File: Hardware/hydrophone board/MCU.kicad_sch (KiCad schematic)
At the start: 1 part, among them U601 RASPBERRY_PI_4B_4GB

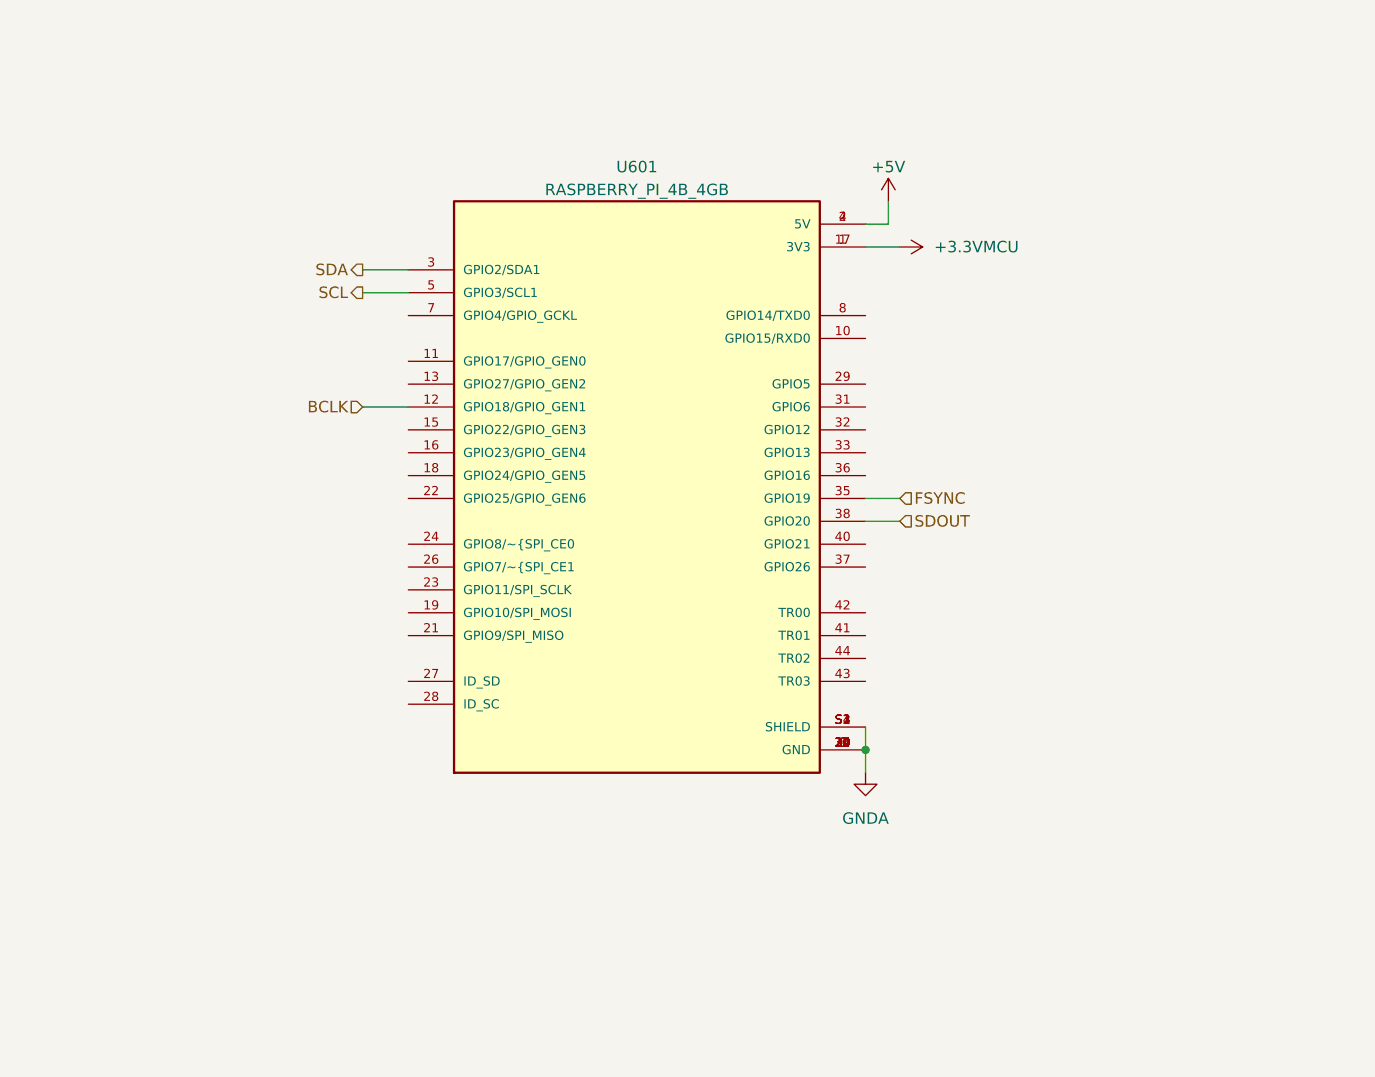
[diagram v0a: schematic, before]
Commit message: i2c pull ups
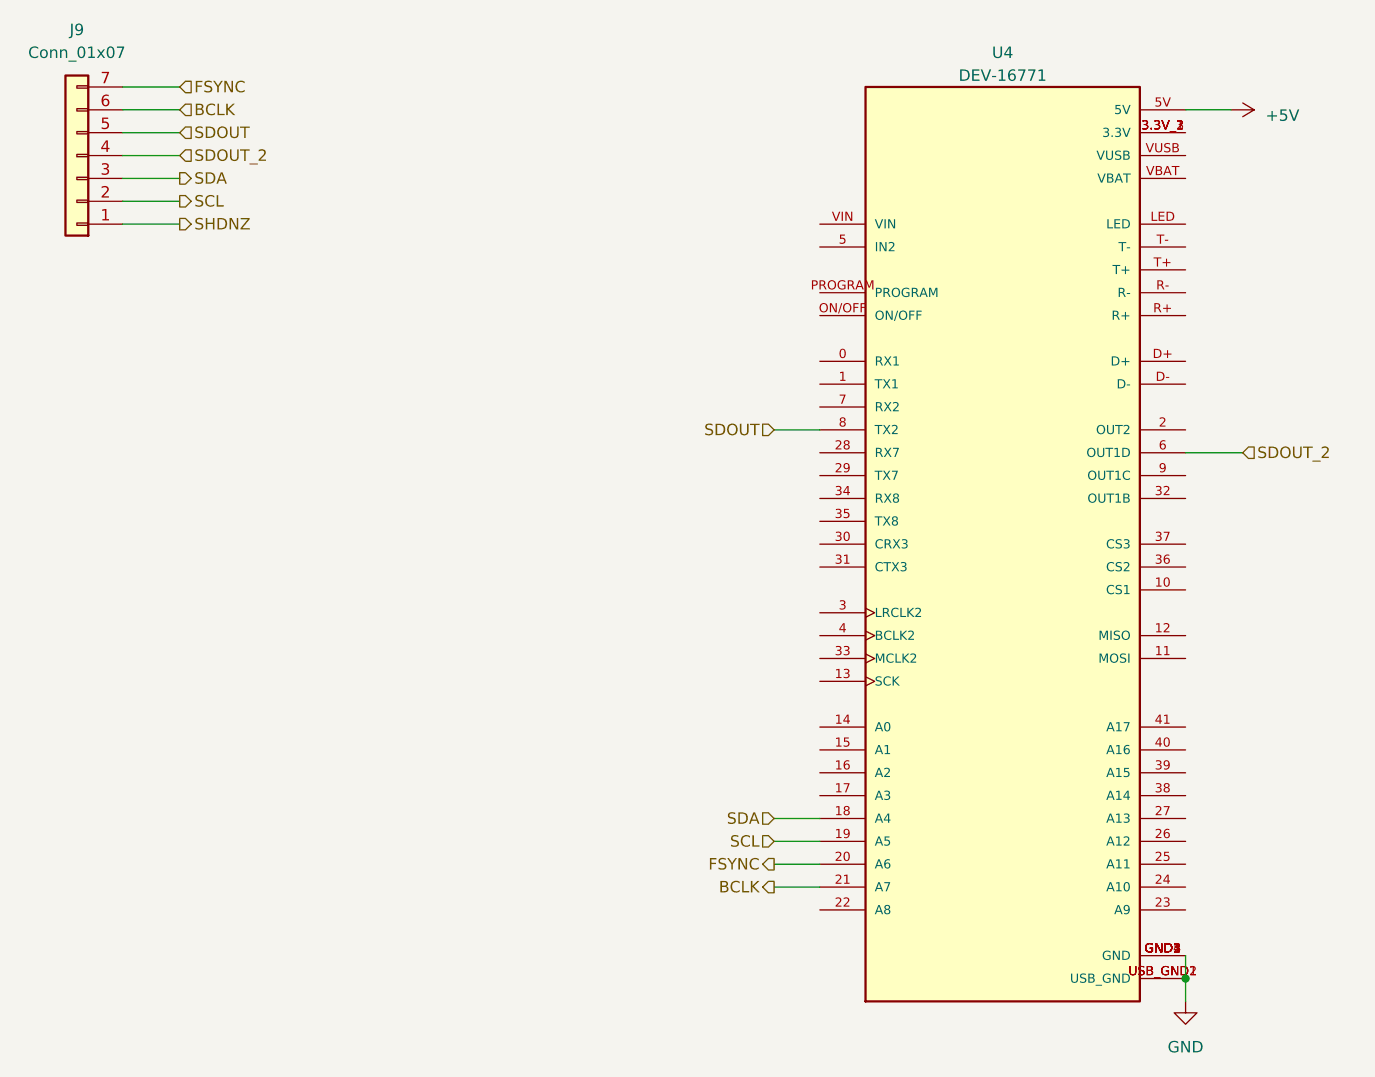
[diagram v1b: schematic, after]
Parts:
- removed U601: RASPBERRY_PI_4B_4GB, RASPBERRY_PI_4B_4GB:MODULE_RASPBERRY_PI_4B_4GB, symbol RASPBERRY_PI_4B_4GB:RASPBERRY_PI_4B_4GB
- added J9: Conn_01x07, symbol Connector_Generic:Conn_01x07
- added U4: DEV-16771, DEV-16771:MODULE_DEV-16771, symbol DEV-16771:DEV-16771
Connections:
- net +5V: now also U4.5V
- net BCLK: now also J9.6 (Pin_6), U4.21 (A7)
- net FSYNC: now also J9.7 (Pin_7), U4.20 (A6)
- net SCL: now also J9.2 (Pin_2), U4.19 (A5)
- net SDA: now also J9.3 (Pin_3), U4.18 (A4)
- net SDOUT: now also J9.5 (Pin_5), U4.8 (TX2)
- new net: U4.3.3V_1 (3.3V), U4.3.3V_2 (3.3V), U4.3.3V_3 (3.3V)
- new net GND: U4.GND1 (GND), U4.GND2 (GND), U4.GND3 (GND), U4.GND4 (GND), U4.GND5 (GND), U4.USB_GND1 (USB_GND), U4.USB_GND2 (USB_GND)
- new net SDOUT_2: J9.4 (Pin_4), U4.6 (OUT1D)
- new net SHDNZ: J9.1 (Pin_1)

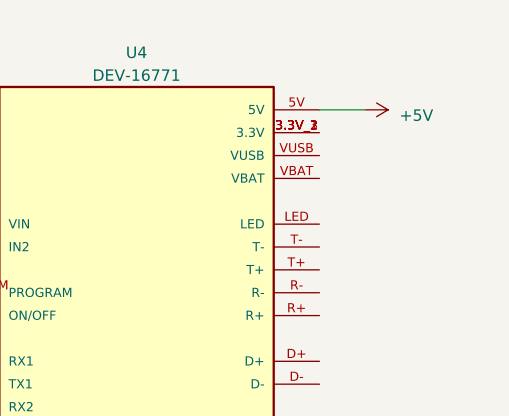
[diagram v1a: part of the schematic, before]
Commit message: 3.3v connector
on power sheet
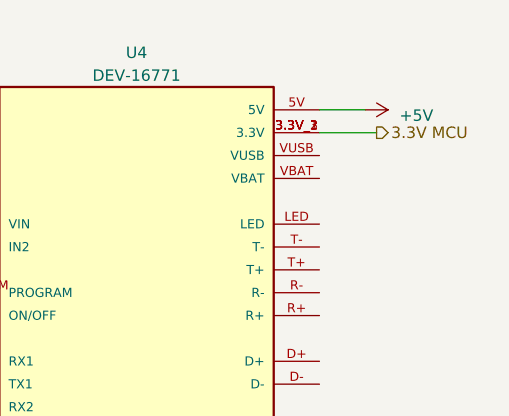
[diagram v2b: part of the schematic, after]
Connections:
- net 3.3V MCU: now reaches U4.3.3V_1 (3.3V), U4.3.3V_2 (3.3V), U4.3.3V_3 (3.3V)
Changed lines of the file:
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@@
   (junction (at 187.96 137.16) (diameter 0) (color 0 0 0 0)
+  )
+  (wire (pts (xy 187.96 43.18) (xy 194.31 43.18))
+    (stroke (width 0) (type default))
   )
   (wire (pts (xy 69.85 50.8) (xy 76.2 50.8))
@@
     (effects (font (size 1.27 1.27)) (justify left))
   )
+  (hierarchical_label "3.3V MCU" (shape output) (at 194.31 43.18 0) (fields_autoplaced)
+    (effects (font (size 1.27 1.27)) (justify left))
+  )

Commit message: Revert "Merge branch 'hardware' of https://github.com/bruin-underwater-robotics/2023-2024 into hardware"
This reverts commit 1d5f0f31a35e539c7b0b2eac7ff2db3bf82506a7, reversing
changes made to b9b3862216192341382b87943b4a1d0c2c46b631.
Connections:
- net 3.3V MCU: no longer names the net of U4.3.3V_1 (3.3V), U4.3.3V_2 (3.3V), U4.3.3V_3 (3.3V)
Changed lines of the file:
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@@
   (junction (at 187.96 137.16) (diameter 0) (color 0 0 0 0)
-  )
-  (wire (pts (xy 187.96 43.18) (xy 194.31 43.18))
-    (stroke (width 0) (type default))
   )
   (wire (pts (xy 69.85 50.8) (xy 76.2 50.8))
@@
     (effects (font (size 1.27 1.27)) (justify left))
   )
-  (hierarchical_label "3.3V MCU" (shape output) (at 194.31 43.18 0) (fields_autoplaced)
-    (effects (font (size 1.27 1.27)) (justify left))
-  )

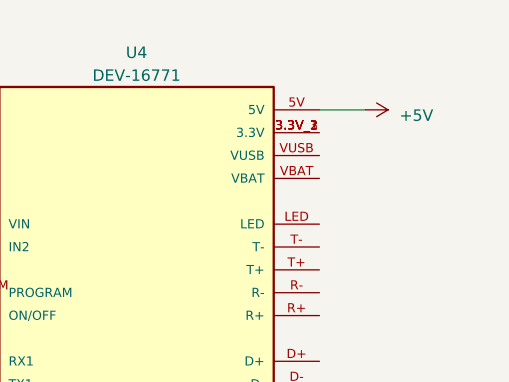
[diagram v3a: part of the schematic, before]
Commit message: changed connectors
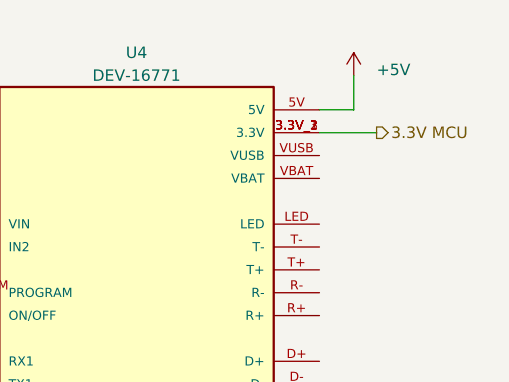
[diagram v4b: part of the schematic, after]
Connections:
- net 3.3V MCU: now reaches U4.3.3V_1 (3.3V), U4.3.3V_2 (3.3V), U4.3.3V_3 (3.3V)
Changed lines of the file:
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@@
+    (stroke (width 0) (type default))
+  )
+  (wire (pts (xy 187.96 43.18) (xy 194.31 43.18))
     (stroke (width 0) (type default))
   )
@@
     (stroke (width 0) (type default))
   )
+  (wire (pts (xy 191.77 40.64) (xy 187.96 40.64))
+    (stroke (width 0) (type default))
+  )
   (wire (pts (xy 142.24 124.46) (xy 147.32 124.46))
     (stroke (width 0) (type default))
@@
     (stroke (width 0) (type default))
   )
-  (wire (pts (xy 187.96 40.64) (xy 193.04 40.64))
+  (wire (pts (xy 191.77 36.83) (xy 191.77 40.64))
     (stroke (width 0) (type default))
   )
@@
   )
   (hierarchical_label "SDA" (shape output) (at 76.2 48.26 0) (fields_autoplaced)
+    (effects (font (size 1.27 1.27)) (justify left))
+  )
+  (hierarchical_label "3.3V MCU" (shape output) (at 194.31 43.18 0) (fields_autoplaced)
     (effects (font (size 1.27 1.27)) (justify left))
   )
@@
     )
   )
-  (symbol (lib_id "power:+5V") (at 193.04 40.64 270) (unit 1)
-    (in_bom yes) (on_board yes) (dnp no) (fields_autoplaced)
-    (property "Reference" "#PWR032" (at 189.23 40.64 0)
-      (effects (font (size 1.27 1.27)) hide)
-    )
-    (property "Value" "+5V" (at 196.85 41.275 90)
+  (symbol (lib_id "power:+5V") (at 191.77 36.83 0) (unit 1)
+    (in_bom yes) (on_board yes) (dnp no) (fields_autoplaced)
+    (property "Reference" "#PWR032" (at 191.77 40.64 0)
+      (effects (font (size 1.27 1.27)) hide)
+    )
+    (property "Value" "+5V" (at 194.31 36.195 0)
       (effects (font (size 1.27 1.27)) (justify left))
     )
-    (property "Footprint" "" (at 193.04 40.64 0)
-      (effects (font (size 1.27 1.27)) hide)
-    )
-    (property "Datasheet" "" (at 193.04 40.64 0)
-      (effects (font (size 1.27 1.27)) hide)
-    )
+    (property "Footprint" "" (at 191.77 36.83 0)
+      (effects (font (size 1.27 1.27)) hide)
+    )
+    (property "Datasheet" "" (at 191.77 36.83 0)
+      (effects (font (size 1.27 1.27)) hide)
+    )

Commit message: annotate all component
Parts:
- renumbered J9 to J301, U4 to U301
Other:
- moved on the sheet: J301
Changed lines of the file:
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@@
   (junction (at 187.96 137.16) (diameter 0) (color 0 0 0 0)
   )
-  (wire (pts (xy 69.85 50.8) (xy 76.2 50.8))
-    (stroke (width 0) (type default))
-  )
-  (wire (pts (xy 69.85 43.18) (xy 76.2 43.18))
+  (wire (pts (xy 80.01 63.5) (xy 86.36 63.5))
+    (stroke (width 0) (type default))
+  )
+  (wire (pts (xy 80.01 55.88) (xy 86.36 55.88))
     (stroke (width 0) (type default))
   )
@@
     (stroke (width 0) (type default))
   )
-  (wire (pts (xy 69.85 40.64) (xy 76.2 40.64))
+  (wire (pts (xy 80.01 53.34) (xy 86.36 53.34))
     (stroke (width 0) (type default))
   )
@@
     (stroke (width 0) (type default))
   )
-  (wire (pts (xy 69.85 38.1) (xy 76.2 38.1))
+  (wire (pts (xy 80.01 50.8) (xy 86.36 50.8))
     (stroke (width 0) (type default))
   )
@@
     (stroke (width 0) (type default))
   )
-  (wire (pts (xy 69.85 53.34) (xy 76.2 53.34))
+  (wire (pts (xy 80.01 66.04) (xy 86.36 66.04))
     (stroke (width 0) (type default))
   )
@@
     (stroke (width 0) (type default))
   )
-  (wire (pts (xy 69.85 45.72) (xy 76.2 45.72))
+  (wire (pts (xy 80.01 58.42) (xy 86.36 58.42))
     (stroke (width 0) (type default))
   )
@@
     (stroke (width 0) (type default))
   )
-  (wire (pts (xy 69.85 48.26) (xy 76.2 48.26))
+  (wire (pts (xy 80.01 60.96) (xy 86.36 60.96))
     (stroke (width 0) (type default))
   )
@@
     (effects (font (size 1.27 1.27)) (justify right))
   )
-  (hierarchical_label "SDA" (shape output) (at 76.2 48.26 0) (fields_autoplaced)
+  (hierarchical_label "SDA" (shape output) (at 86.36 60.96 0) (fields_autoplaced)
     (effects (font (size 1.27 1.27)) (justify left))
   )
@@
     (effects (font (size 1.27 1.27)) (justify left))
   )
-  (hierarchical_label "SHDNZ" (shape output) (at 76.2 53.34 0) (fields_autoplaced)
+  (hierarchical_label "SHDNZ" (shape output) (at 86.36 66.04 0) (fields_autoplaced)
     (effects (font (size 1.27 1.27)) (justify left))
   )
@@
     (effects (font (size 1.27 1.27)) (justify left))
   )
-  (hierarchical_label "SCL" (shape output) (at 76.2 50.8 0) (fields_autoplaced)
-    (effects (font (size 1.27 1.27)) (justify left))
-  )
-  (hierarchical_label "SDOUT" (shape input) (at 76.2 43.18 0) (fields_autoplaced)
-    (effects (font (size 1.27 1.27)) (justify left))
-  )
-  (hierarchical_label "BCLK" (shape input) (at 76.2 40.64 0) (fields_autoplaced)
-    (effects (font (size 1.27 1.27)) (justify left))
-  )
-  (hierarchical_label "FSYNC" (shape input) (at 76.2 38.1 0) (fields_autoplaced)
+  (hierarchical_label "SCL" (shape output) (at 86.36 63.5 0) (fields_autoplaced)
+    (effects (font (size 1.27 1.27)) (justify left))
+  )
+  (hierarchical_label "SDOUT" (shape input) (at 86.36 55.88 0) (fields_autoplaced)
+    (effects (font (size 1.27 1.27)) (justify left))
+  )
+  (hierarchical_label "BCLK" (shape input) (at 86.36 53.34 0) (fields_autoplaced)
+    (effects (font (size 1.27 1.27)) (justify left))
+  )
+  (hierarchical_label "FSYNC" (shape input) (at 86.36 50.8 0) (fields_autoplaced)
     (effects (font (size 1.27 1.27)) (justify left))
   )
@@
     (effects (font (size 1.27 1.27)) (justify right))
   )
-  (hierarchical_label "SDOUT_2" (shape input) (at 76.2 45.72 0) (fields_autoplaced)
+  (hierarchical_label "SDOUT_2" (shape input) (at 86.36 58.42 0) (fields_autoplaced)
     (effects (font (size 1.27 1.27)) (justify left))
   )
   (symbol (lib_id "DEV-16771:DEV-16771") (at 167.64 88.9 0) (unit 1)
     (in_bom yes) (on_board yes) (dnp no) (fields_autoplaced)
-    (property "Reference" "U4" (at 167.64 34.29 0)
+    (property "Reference" "U301" (at 167.64 34.29 0)
       (effects (font (size 1.27 1.27)))
     )
@@
       (project "hydrophone board"
         (path "/4356d3a6-6a00-447d-897e-473f60221539/1c2c9d85-5695-48de-99af-3ac5f27a43fe"
-          (reference "U4") (unit 1)
+          (reference "U301") (unit 1)
         )
       )
     )
   )
-  (symbol (lib_id "Connector_Generic:Conn_01x07") (at 64.77 45.72 180) (unit 1)
+  (symbol (lib_id "Connector_Generic:Conn_01x07") (at 74.93 58.42 180) (unit 1)
     (in_bom yes) (on_board yes) (dnp no) (fields_autoplaced)
-    (property "Reference" "J9" (at 64.77 31.75 0)
-      (effects (font (size 1.27 1.27)))
-    )
-    (property "Value" "Conn_01x07" (at 64.77 34.29 0)
-      (effects (font (size 1.27 1.27)))
-    )
-    (property "Footprint" "" (at 64.77 45.72 0)
-      (effects (font (size 1.27 1.27)) hide)
-    )
-    (property "Datasheet" "~" (at 64.77 45.72 0)
+    (property "Reference" "J301" (at 74.93 44.45 0)
+      (effects (font (size 1.27 1.27)))
+    )
+    (property "Value" "Conn_01x07" (at 74.93 46.99 0)
+      (effects (font (size 1.27 1.27)))
+    )
+    (property "Footprint" "" (at 74.93 58.42 0)
+      (effects (font (size 1.27 1.27)) hide)
+    )
+    (property "Datasheet" "~" (at 74.93 58.42 0)
       (effects (font (size 1.27 1.27)) hide)
     )
@@
       (project "hydrophone board"
         (path "/4356d3a6-6a00-447d-897e-473f60221539/1c2c9d85-5695-48de-99af-3ac5f27a43fe"
-          (reference "J9") (unit 1)
+          (reference "J301") (unit 1)
         )
       )
@@
   (symbol (lib_id "PCM_4ms_Power-symbol:GND") (at 187.96 139.7 0) (unit 1)
     (in_bom yes) (on_board yes) (dnp no) (fields_autoplaced)
-    (property "Reference" "#PWR040" (at 187.96 146.05 0)
+    (property "Reference" "#PWR0302" (at 187.96 146.05 0)
       (effects (font (size 1.27 1.27)) hide)
     )
@@
       (project "hydrophone board"
         (path "/4356d3a6-6a00-447d-897e-473f60221539/1c2c9d85-5695-48de-99af-3ac5f27a43fe"
-          (reference "#PWR040") (unit 1)
+          (reference "#PWR0302") (unit 1)
         )
       )
@@
         )
         (path "/4356d3a6-6a00-447d-897e-473f60221539/1c2c9d85-5695-48de-99af-3ac5f27a43fe"
-          (reference "#PWR032") (unit 1)
+          (reference "#PWR0301") (unit 1)
         )
       )

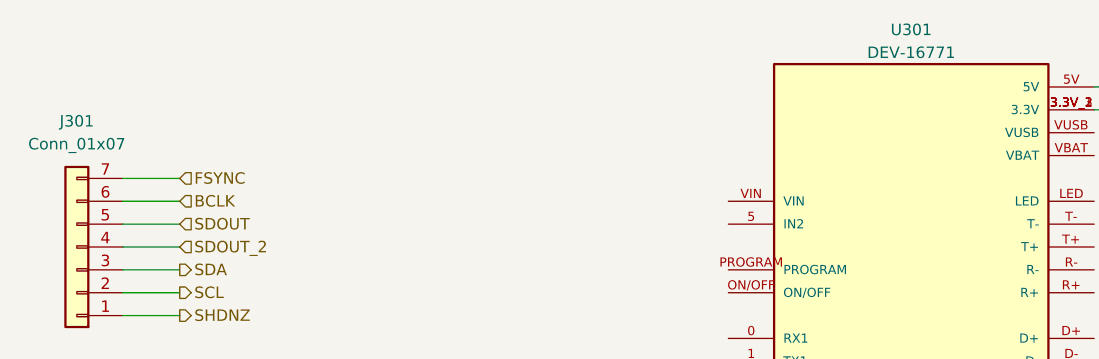
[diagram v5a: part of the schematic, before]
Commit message: assigned footprints
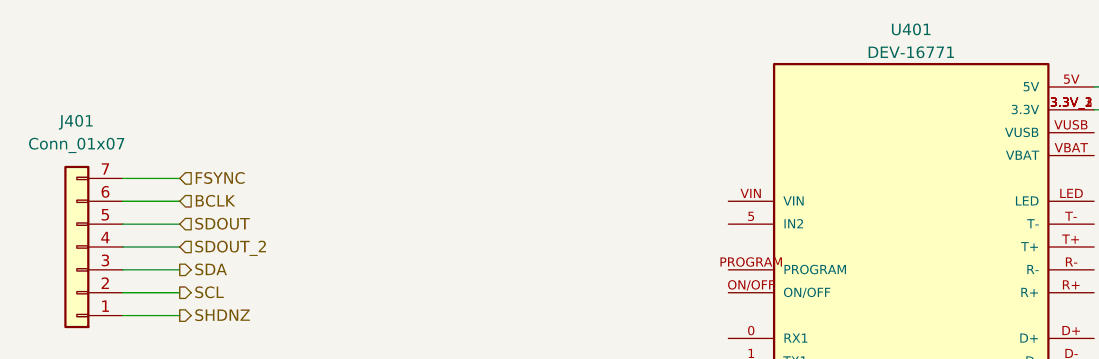
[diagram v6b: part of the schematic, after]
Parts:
- J401: renamed from J301; footprint (none) -> Connector_PinHeader_2.54mm:PinHeader_1x07_P2.54mm_Vertical
- renumbered U301 to U401
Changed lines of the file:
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@@
   (symbol (lib_id "DEV-16771:DEV-16771") (at 167.64 88.9 0) (unit 1)
     (in_bom yes) (on_board yes) (dnp no) (fields_autoplaced)
-    (property "Reference" "U301" (at 167.64 34.29 0)
+    (property "Reference" "U401" (at 167.64 34.29 0)
       (effects (font (size 1.27 1.27)))
     )
@@
       (project "hydrophone board"
         (path "/4356d3a6-6a00-447d-897e-473f60221539/1c2c9d85-5695-48de-99af-3ac5f27a43fe"
-          (reference "U301") (unit 1)
+          (reference "U401") (unit 1)
         )
       )
@@
   (symbol (lib_id "Connector_Generic:Conn_01x07") (at 74.93 58.42 180) (unit 1)
     (in_bom yes) (on_board yes) (dnp no) (fields_autoplaced)
-    (property "Reference" "J301" (at 74.93 44.45 0)
+    (property "Reference" "J401" (at 74.93 44.45 0)
       (effects (font (size 1.27 1.27)))
     )
@@
       (effects (font (size 1.27 1.27)))
     )
-    (property "Footprint" "" (at 74.93 58.42 0)
+    (property "Footprint" "Connector_PinHeader_2.54mm:PinHeader_1x07_P2.54mm_Vertical" (at 74.93 58.42 0)
       (effects (font (size 1.27 1.27)) hide)
     )
@@
       (project "hydrophone board"
         (path "/4356d3a6-6a00-447d-897e-473f60221539/1c2c9d85-5695-48de-99af-3ac5f27a43fe"
-          (reference "J301") (unit 1)
+          (reference "J401") (unit 1)
         )
       )
@@
   (symbol (lib_id "PCM_4ms_Power-symbol:GND") (at 187.96 139.7 0) (unit 1)
     (in_bom yes) (on_board yes) (dnp no) (fields_autoplaced)
-    (property "Reference" "#PWR0302" (at 187.96 146.05 0)
+    (property "Reference" "#PWR0402" (at 187.96 146.05 0)
       (effects (font (size 1.27 1.27)) hide)
     )
@@
       (project "hydrophone board"
         (path "/4356d3a6-6a00-447d-897e-473f60221539/1c2c9d85-5695-48de-99af-3ac5f27a43fe"
-          (reference "#PWR0302") (unit 1)
+          (reference "#PWR0402") (unit 1)
         )
       )
@@
         )
         (path "/4356d3a6-6a00-447d-897e-473f60221539/1c2c9d85-5695-48de-99af-3ac5f27a43fe"
-          (reference "#PWR0301") (unit 1)
-        )
-      )
+          (reference "#PWR0401") (unit 1)
+        )
+      )
